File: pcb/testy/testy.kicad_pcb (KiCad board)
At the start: 2 copper layers, 180.9 x 103.6 mm, 44 parts, among them U1 ProMicro

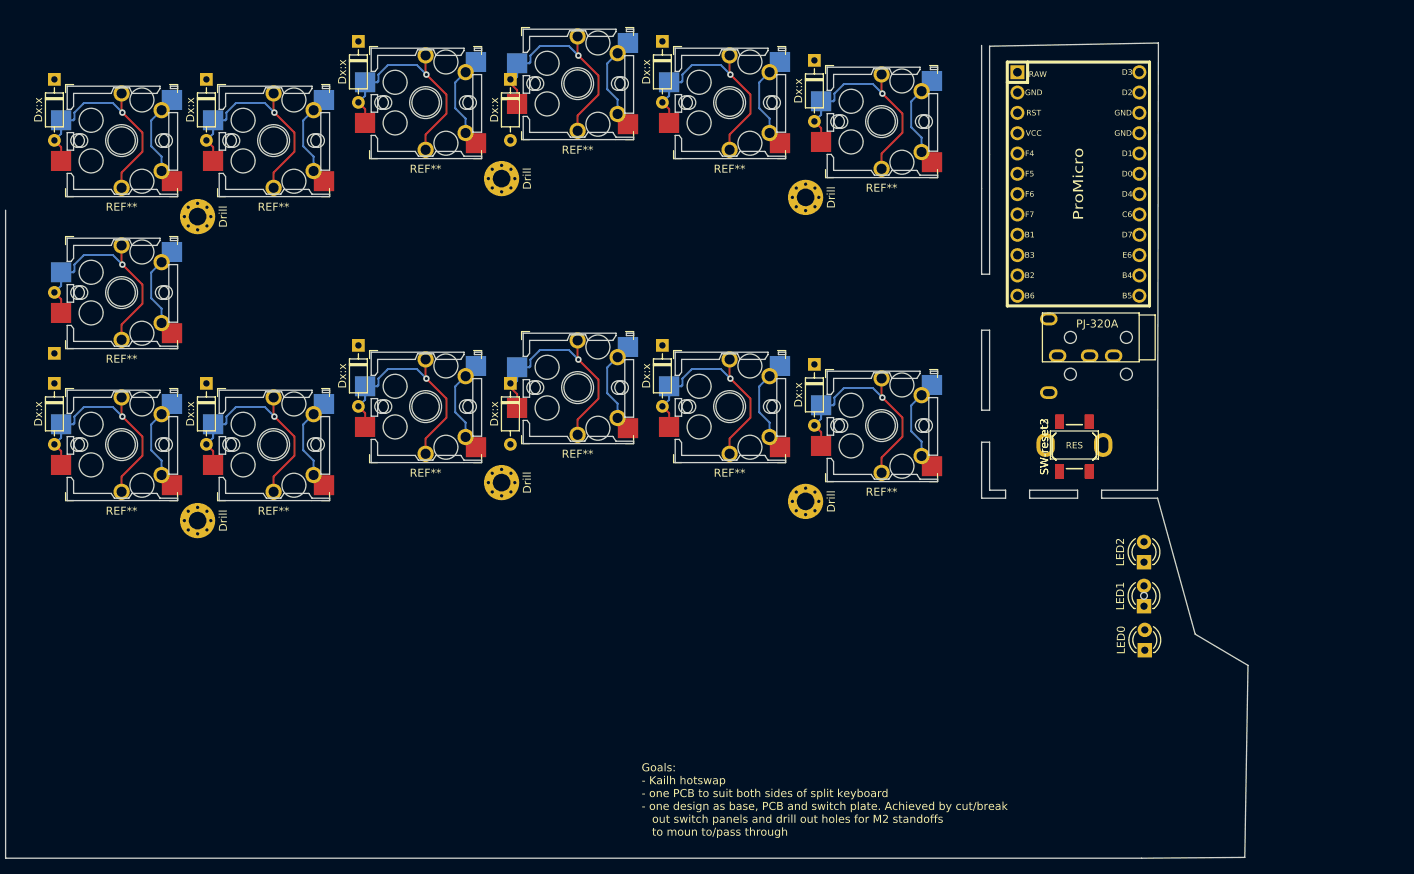
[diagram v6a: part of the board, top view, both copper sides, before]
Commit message: feat: complete key layout
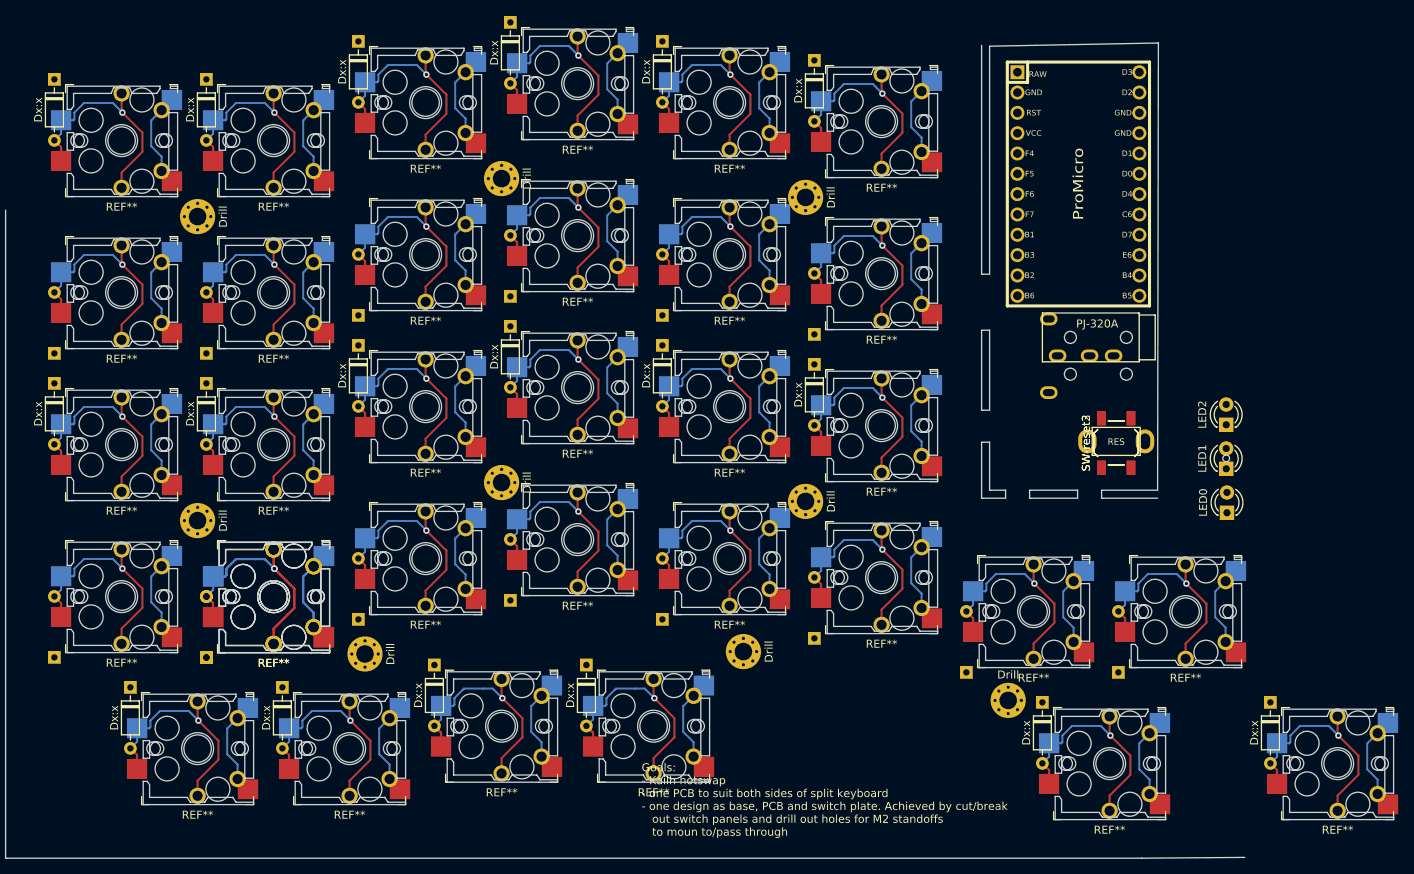
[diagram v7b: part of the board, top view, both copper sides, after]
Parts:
- removed the Dx:x at (117.1, 25.6)
- removed the Dx:x at (117.1, 63.6)
- added Drill: MountingHole_2.2mm_M2_Pad_Via, MountingHole:MountingHole_2.2mm_M2_Pad_Via, F.Cu at (179.3, 103.3)
- added Drill: MountingHole_2.2mm_M2_Pad_Via, MountingHole:MountingHole_2.2mm_M2_Pad_Via, F.Cu at (146.2, 97.2)
- added Drill: MountingHole_2.2mm_M2_Pad_Via, MountingHole:MountingHole_2.2mm_M2_Pad_Via, F.Cu at (98.9, 97.5)
- added Dx:x: 1N4148, Diode_THT:D_DO-35_SOD27_P7.62mm_Horizontal, F.Cu at (212.1, 103.5)
- added Dx:x: 1N4148, Diode_THT:D_DO-35_SOD27_P7.62mm_Horizontal, B.Cu at (136.1, 93.2)
- added Dx:x: 1N4148, Diode_THT:D_DO-35_SOD27_P7.62mm_Horizontal, B.Cu at (117.1, 90.8)
- added Dx:x: 1N4148, Diode_THT:D_DO-35_SOD27_P7.62mm_Horizontal, B.Cu at (98.1, 93.2)
- added Dx:x (x2): 1N4148, Diode_THT:D_DO-35_SOD27_P7.62mm_Horizontal, B.Cu at (79.1, 97.9)
- added Dx:x: 1N4148, Diode_THT:D_DO-35_SOD27_P7.62mm_Horizontal, B.Cu at (60.1, 97.9)
- added Dx:x: 1N4148, Diode_THT:D_DO-35_SOD27_P7.62mm_Horizontal, F.Cu at (117.1, 56.5)
- added Dx:x: 1N4148, Diode_THT:D_DO-35_SOD27_P7.62mm_Horizontal, F.Cu at (117.1, 18.5)
- added Dx:x: 1N4148, Diode_THT:D_DO-35_SOD27_P7.62mm_Horizontal, B.Cu at (155.1, 57.5)
- added Dx:x: 1N4148, Diode_THT:D_DO-35_SOD27_P7.62mm_Horizontal, B.Cu at (136.1, 55.1)
- added Dx:x: 1N4148, Diode_THT:D_DO-35_SOD27_P7.62mm_Horizontal, B.Cu at (193.1, 99.8)
- added Dx:x: 1N4148, Diode_THT:D_DO-35_SOD27_P7.62mm_Horizontal, B.Cu at (117.1, 52.8)
- added Dx:x: 1N4148, Diode_THT:D_DO-35_SOD27_P7.62mm_Horizontal, B.Cu at (98.1, 55.1)
- added Dx:x: 1N4148, Diode_THT:D_DO-35_SOD27_P7.62mm_Horizontal, B.Cu at (79.1, 59.9)
- added Dx:x: 1N4148, Diode_THT:D_DO-35_SOD27_P7.62mm_Horizontal, F.Cu at (183.6, 103.5)
- added Dx:x: 1N4148, Diode_THT:D_DO-35_SOD27_P7.62mm_Horizontal, B.Cu at (174.1, 99.8)
- added Dx:x: 1N4148, Diode_THT:D_DO-35_SOD27_P7.62mm_Horizontal, F.Cu at (126.6, 98.8)
- added Dx:x: 1N4148, Diode_THT:D_DO-35_SOD27_P7.62mm_Horizontal, F.Cu at (107.6, 98.8)
- added Dx:x: 1N4148, Diode_THT:D_DO-35_SOD27_P7.62mm_Horizontal, F.Cu at (88.6, 101.7)
- added Dx:x: 1N4148, Diode_THT:D_DO-35_SOD27_P7.62mm_Horizontal, F.Cu at (69.6, 101.7)
- added Dx:x: 1N4148, Diode_THT:D_DO-35_SOD27_P7.62mm_Horizontal, B.Cu at (155.1, 95.5)
- added REF**: PG1511_socket, footprints:kailh-socket-and-choc-solder-reversible, F.Cu at (220.5, 111.2)
- added REF**: PG1511_socket, footprints:kailh-socket-and-choc-solder-reversible, F.Cu at (144.5, 85.5)
- added REF**: PG1511_socket, footprints:kailh-socket-and-choc-solder-reversible, F.Cu at (125.5, 83.2)
- added REF**: PG1511_socket, footprints:kailh-socket-and-choc-solder-reversible, F.Cu at (106.5, 85.5)
- added REF** (x2): PG1511_socket, footprints:kailh-socket-and-choc-solder-reversible, F.Cu at (87.5, 90.3)
- added REF**: PG1511_socket, footprints:kailh-socket-and-choc-solder-reversible, F.Cu at (68.5, 90.3)
- added REF**: PG1511_socket, footprints:kailh-socket-and-choc-solder-reversible, F.Cu at (163.5, 49.9)
- added REF**: PG1511_socket, footprints:kailh-socket-and-choc-solder-reversible, F.Cu at (144.5, 47.5)
- added REF**: PG1511_socket, footprints:kailh-socket-and-choc-solder-reversible, F.Cu at (201.5, 92.2)
- added REF**: PG1511_socket, footprints:kailh-socket-and-choc-solder-reversible, F.Cu at (125.5, 45.2)
- added REF**: PG1511_socket, footprints:kailh-socket-and-choc-solder-reversible, F.Cu at (106.5, 47.5)
- added REF**: PG1511_socket, footprints:kailh-socket-and-choc-solder-reversible, F.Cu at (87.5, 52.3)
- added REF**: PG1511_socket, footprints:kailh-socket-and-choc-solder-reversible, F.Cu at (192.0, 111.2)
- added REF**: PG1511_socket, footprints:kailh-socket-and-choc-solder-reversible, F.Cu at (182.5, 92.2)
- added REF**: PG1511_socket, footprints:kailh-socket-and-choc-solder-reversible, F.Cu at (135.0, 106.5)
- added REF**: PG1511_socket, footprints:kailh-socket-and-choc-solder-reversible, F.Cu at (116.0, 106.5)
- added REF**: PG1511_socket, footprints:kailh-socket-and-choc-solder-reversible, F.Cu at (97.0, 109.3)
- added REF**: PG1511_socket, footprints:kailh-socket-and-choc-solder-reversible, F.Cu at (78.0, 109.3)
- added REF**: PG1511_socket, footprints:kailh-socket-and-choc-solder-reversible, F.Cu at (163.5, 87.9)
- moved LED0 20.0 mm to (206.7, 79.8)
- moved LED1 20.0 mm to (206.6, 74.3)
- moved LED2 20.0 mm to (206.6, 68.8)
- moved SW-reset2 5.24 mm to (192.8, 71.1)
- moved SW-reset3 5.24 mm to (192.8, 71.1)
- moved SW-reset1 5.24 mm to (192.8, 72.7)
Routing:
- net (no net): track 621.7 -> 1450.5 mm, vias 15 -> 35
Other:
- board size 180.9 x 103.6 mm -> 199.1 x 103.6 mm

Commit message: chore: tidy up PCB, still lots of errors
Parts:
- removed the Dx:x at (26.9, 73.5)
- removed the Dx:x at (30.6, 68.0)
- removed the REF** at (35.2, 81.2)
- removed the REF** at (39.0, 60.4)
- added Drill: MountingHole_2.2mm_M2_Pad_Via, MountingHole:MountingHole_2.2mm_M2_Pad_Via, F.Cu at (220.2, 141.8)
- added Drill: MountingHole_2.2mm_M2_Pad_Via, MountingHole:MountingHole_2.2mm_M2_Pad_Via, F.Cu at (230.5, 123.6)
- SW-reset3: moved to B.Cu
- moved SW-reset1 37.3 mm to (216.2, 101.7)
- moved SW-reset2 37.3 mm to (216.2, 100.1)
- moved SW-reset3 37.3 mm to (216.2, 100.1), turned to 270 degrees
- moved LED2 31.8 mm to (196.5, 99.0), turned to 180 degrees
- moved REF** 31.2 mm to (110.7, 137.3)
- moved REF** 31.2 mm to (91.7, 137.3)
- moved Dx:x 31.2 mm to (130.8, 84.5)
- moved Dx:x 31.2 mm to (168.8, 85.5)
- moved Dx:x 31.2 mm to (149.8, 83.2)
- moved Dx:x 31.2 mm to (130.8, 80.8)
- moved Dx:x 31.2 mm to (168.8, 89.3)
- moved Dx:x 31.2 mm to (149.8, 86.9)
- moved Dx:x 31.2 mm to (111.8, 83.2)
- moved Dx:x 31.2 mm to (92.8, 87.9)
- moved Dx:x 31.2 mm to (92.8, 91.7)
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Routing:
- net GND: track 0.00 -> 88.0 mm
- net (no net): track 1450.5 -> 1367.8 mm, vias 35 -> 33
- net Reset: track 0.00 -> 16.1 mm
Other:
- board size 199.1 x 103.6 mm -> 175 x 108 mm
- board text removed: "Goals: - Kailh hotswap - one PCB to suit both sides of split keyboard - one design as base, PCB and switch plate. Achieved by cut/break out switch panels and drill out holes for M2 standoffs to moun to/pass through"
- board text removed: "Ignore us, we're just templates"
